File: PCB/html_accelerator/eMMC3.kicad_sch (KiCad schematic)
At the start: 16 parts, among them U2 AU6438BS, U5 EMMC_4G, U6 EMMC_4G, U7 EMMC_4G, Y1 12MHz

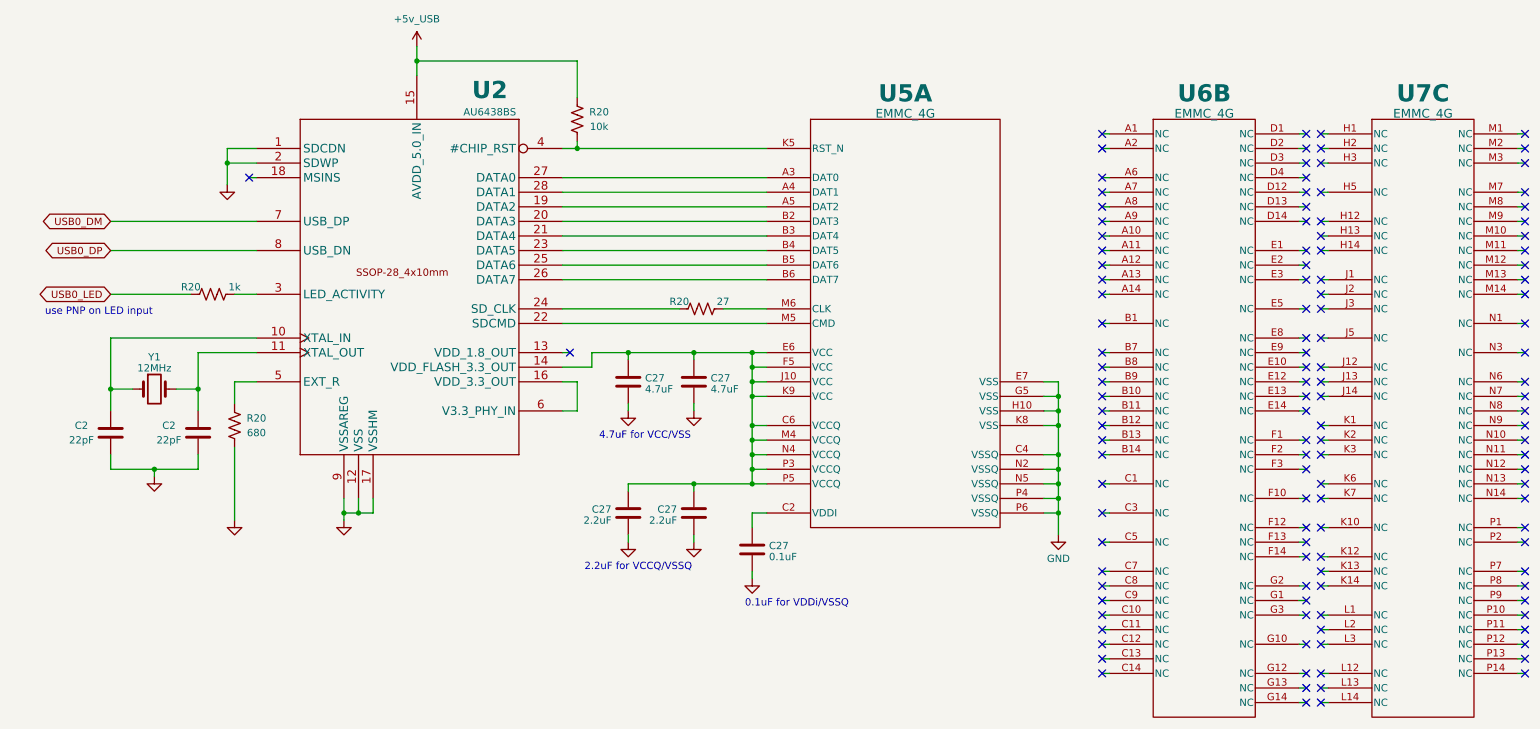
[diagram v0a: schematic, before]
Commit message: EMMC symbols and netlist
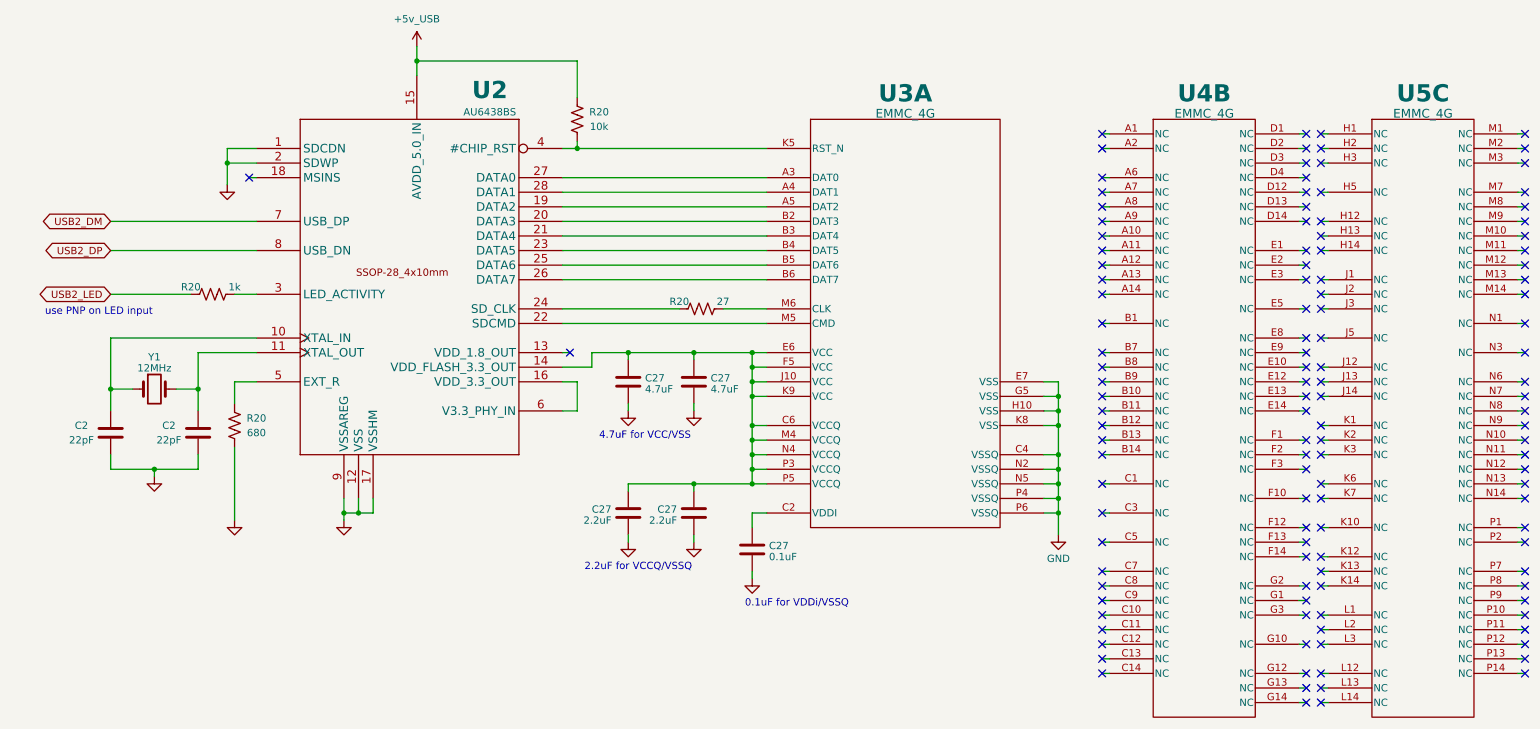
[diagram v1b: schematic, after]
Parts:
- removed C2 (x2): 22pF, symbol Device:C
- removed C27 (x2): 2.2uF, symbol Device:C
- removed C27 (x2): 4.7uF, symbol Device:C
- removed C27: 0.1uF, symbol Device:C
- removed R20: 10k, symbol Device:R_US
- removed R20: 680, symbol Device:R_US
- removed R20: 1k, symbol Device:R_US
- removed R20: 27, symbol Device:R_US
- removed U5, U6, U7: EMMC_4G, EMMC04G-M627-X03U_KNT, symbol html_accel_Symbols:EMMC_4G
- added C2 (x2): 22pF, symbol Device:C
- added C27 (x2): 2.2uF, symbol Device:C
- added C27: 0.1uF, symbol Device:C
- added C27 (x2): 4.7uF, symbol Device:C
- added R20: 680, symbol Device:R_US
- added R20: 1k, symbol Device:R_US
- added R20: 10k, symbol Device:R_US
- added R20: 27, symbol Device:R_US
- added U3, U4, U5: EMMC_4G, EMMC04G-M627-X03U_KNT, symbol html_accel_Symbols:EMMC_4G
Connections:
- net +3V3: now also R20.1
- net GND: now also C2.2, C2.2, C27.2, C27.2, C27.2, C27.2, C27.2, R20.2, U3.C4 (VSSQ), U3.E7 (VSS), U3.G5 (VSS), U3.H10 (VSS), U3.K8 (VSS), U3.N2 (VSSQ), U3.N5 (VSSQ), U3.P4 (VSSQ), U3.P6 (VSSQ)
- net at U2.4 (#CHIP_RST): now also R20.2, U3.K5 (RST_N)
- net at U2.27 (DATA0): now also U3.A3 (DAT0)
- net at U2.28 (DATA1): now also U3.A4 (DAT1)
- net at U2.19 (DATA2): now also U3.A5 (DAT2)
- net at U2.20 (DATA3): now also U3.B2 (DAT3)
- net at U2.21 (DATA4): now also U3.B3 (DAT4)
- net at U2.23 (DATA5): now also U3.B4 (DAT5)
- net at U2.25 (DATA6): now also U3.B5 (DAT6)
- net at U2.26 (DATA7): now also U3.B6 (DAT7)
- net at U2.14 (VDD_FLASH_3.3_OUT): now also C27.1, C27.1, C27.1, C27.1, U3.C6 (VCCQ), U3.E6 (VCC), U3.F5 (VCC), U3.J10 (VCC), U3.K9 (VCC), U3.M4 (VCCQ), U3.N4 (VCCQ), U3.P3 (VCCQ), U3.P5 (VCCQ)
- net at U2.22 (SDCMD): now also U3.M5 (CMD)
- net at U2.5 (EXT_R): now also R20.1
- net at U2.11 (XTAL_OUT), Y1.2: now also C2.1
- net at U2.10 (XTAL_IN), Y1.1: now also C2.1
- net at U2.3 (LED_ACTIVITY): now also R20.2
- net at U2.24 (SD_CLK): now also R20.1
- net USB0_DM renamed USB2_DM
- net USB0_DP renamed USB2_DP
- new net: C27.1, U3.C2 (VDDI)
- new net: R20.2, U3.M6 (CLK)
- new net USB2_LED: R20.1

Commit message: 3d part models, PCB netlist imported
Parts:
- C2, C27: footprint (none) -> Capacitor_SMD:C_0805_2012Metric_Pad1.18x1.45mm_HandSolder
- R20: footprint (none) -> Resistor_SMD:R_0805_2012Metric_Pad1.20x1.40mm_HandSolder
- U3, U4, U5: footprint EMMC04G-M627-X03U_KNT -> html_accel_footprints:EMMC04G-M627-X03U_KNT
- Y1: footprint (none) -> Crystal:Crystal_SMD_HC49-SD
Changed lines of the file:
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@@
       (effects (font (size 1.524 1.524)))
     )
-    (property "Footprint" "EMMC04G-M627-X03U_KNT" (at 231.14 48.26 0)
+    (property "Footprint" "html_accel_footprints:EMMC04G-M627-X03U_KNT" (at 231.14 48.26 0)
       (effects (font (size 1.27 1.27) italic) hide)
     )
@@
       (effects (font (size 1.27 1.27)))
     )
-    (property "Footprint" "" (at 48.5648 106.68 0)
+    (property "Footprint" "Capacitor_SMD:C_0805_2012Metric_Pad1.18x1.45mm_HandSolder" (at 48.5648 106.68 0)
       (effects (font (size 1.27 1.27)) hide)
     )
@@
       (effects (font (size 1.27 1.27)))
     )
-    (property "Footprint" "" (at 56.896 101.854 90)
+    (property "Footprint" "Resistor_SMD:R_0805_2012Metric_Pad1.20x1.40mm_HandSolder" (at 56.896 101.854 90)
       (effects (font (size 1.27 1.27)) hide)
     )
@@
       (effects (font (size 1.27 1.27)) (justify left))
     )
-    (property "Footprint" "" (at 134.9248 120.65 0)
+    (property "Footprint" "Capacitor_SMD:C_0805_2012Metric_Pad1.18x1.45mm_HandSolder" (at 134.9248 120.65 0)
       (effects (font (size 1.27 1.27)) hide)
     )
@@
       (effects (font (size 1.27 1.27)))
     )
-    (property "Footprint" "" (at 52.324 77.724 90)
+    (property "Footprint" "Resistor_SMD:R_0805_2012Metric_Pad1.20x1.40mm_HandSolder" (at 52.324 77.724 90)
       (effects (font (size 1.27 1.27)) hide)
     )
@@
       (effects (font (size 1.27 1.27)) (justify left))
     )
-    (property "Footprint" "" (at 147.0152 127 0)
+    (property "Footprint" "Capacitor_SMD:C_0805_2012Metric_Pad1.18x1.45mm_HandSolder" (at 147.0152 127 0)
       (effects (font (size 1.27 1.27)) hide)
     )
@@
       (effects (font (size 1.524 1.524)))
     )
-    (property "Footprint" "EMMC04G-M627-X03U_KNT" (at 171.45 48.26 0)
+    (property "Footprint" "html_accel_footprints:EMMC04G-M627-X03U_KNT" (at 171.45 48.26 0)
       (effects (font (size 1.27 1.27) italic) hide)
     )
@@
       (effects (font (size 1.27 1.27)))
     )
-    (property "Footprint" "" (at 33.3248 106.68 0)
+    (property "Footprint" "Capacitor_SMD:C_0805_2012Metric_Pad1.18x1.45mm_HandSolder" (at 33.3248 106.68 0)
       (effects (font (size 1.27 1.27)) hide)
     )
@@
       (effects (font (size 1.524 1.524)))
     )
-    (property "Footprint" "EMMC04G-M627-X03U_KNT" (at 269.24 48.26 0)
+    (property "Footprint" "html_accel_footprints:EMMC04G-M627-X03U_KNT" (at 269.24 48.26 0)
       (effects (font (size 1.27 1.27) italic) hide)
     )
@@
       (effects (font (size 1.27 1.27)))
     )
-    (property "Footprint" "" (at 116.586 48.514 90)
+    (property "Footprint" "Resistor_SMD:R_0805_2012Metric_Pad1.20x1.40mm_HandSolder" (at 116.586 48.514 90)
       (effects (font (size 1.27 1.27)) hide)
     )
@@
       (effects (font (size 1.27 1.27)) (justify left))
     )
-    (property "Footprint" "" (at 123.4948 120.65 0)
+    (property "Footprint" "Capacitor_SMD:C_0805_2012Metric_Pad1.18x1.45mm_HandSolder" (at 123.4948 120.65 0)
       (effects (font (size 1.27 1.27)) hide)
     )
@@
       (effects (font (size 1.27 1.27)))
     )
-    (property "Footprint" "" (at 41.91 95.25 0)
-      (effects (font (size 1.27 1.27)) hide)
-    )
-    (property "Datasheet" "~" (at 41.91 95.25 0)
+    (property "Footprint" "Crystal:Crystal_SMD_HC49-SD" (at 41.91 95.25 0)
+      (effects (font (size 1.27 1.27)) hide)
+    )
+    (property "Datasheet" "12M20P2/49SMT" (at 41.91 95.25 0)
       (effects (font (size 1.27 1.27)) hide)
     )
@@
       (effects (font (size 1.27 1.27)) (justify left))
     )
-    (property "Footprint" "" (at 136.8552 97.79 0)
+    (property "Footprint" "Capacitor_SMD:C_0805_2012Metric_Pad1.18x1.45mm_HandSolder" (at 136.8552 97.79 0)
       (effects (font (size 1.27 1.27)) hide)
     )
@@
       (effects (font (size 1.27 1.27)))
     )
-    (property "Footprint" "" (at 137.414 80.264 90)
+    (property "Footprint" "Resistor_SMD:R_0805_2012Metric_Pad1.20x1.40mm_HandSolder" (at 137.414 80.264 90)
       (effects (font (size 1.27 1.27)) hide)
     )
@@
       (effects (font (size 1.27 1.27)) (justify left))
     )
-    (property "Footprint" "" (at 125.4252 97.79 0)
-      (effects (font (size 1.27 1.27)) hide)
-    )
+    (property "Footprint" "Capacitor_SMD:C_0805_2012Metric_Pad1.18x1.45mm_HandSolder" (at 125.4252 97.79 0)
+      (effects (font (size 1.27 1.27)) hide)
+    )

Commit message: placement updates
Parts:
- Y1: footprint Crystal:Crystal_SMD_HC49-SD -> Crystal:Crystal_SMD_3225-4Pin_3.2x2.5mm
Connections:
- net +3V3 renamed +5V
- no-connect marks 125 -> 2

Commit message: layout and 3d updates
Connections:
- net DATA_2: now reaches U2.19 (DATA2), U3.A5 (DAT2)
- net DATA_3: now reaches U2.20 (DATA3), U3.B2 (DAT3)
- net DATA_4: now reaches U2.21 (DATA4), U3.B3 (DAT4)
- net DATA_5: now reaches U2.23 (DATA5), U3.B4 (DAT5)
- net DATA_6: now reaches U2.25 (DATA6), U3.B5 (DAT6)
- net DATA_7: now reaches U2.26 (DATA7), U3.B6 (DAT7)
- net DATA_0: now reaches U2.27 (DATA0), U3.A3 (DAT0)
- net DATA_1: now reaches U2.28 (DATA1), U3.A4 (DAT1)
- net USB2_DM renamed 90_USB2_D_P
- net USB2_DP renamed 90_USB2_D_N
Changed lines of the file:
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@@
+    (effects (font (size 1.27 1.27)) (justify left bottom))
+  )
+  (label "DATA_0" (at 115.57 58.42 0) (fields_autoplaced)
+    (effects (font (size 1.27 1.27)) (justify left bottom))
+  )
+  (label "DATA_1" (at 115.57 60.96 0) (fields_autoplaced)
+    (effects (font (size 1.27 1.27)) (justify left bottom))
+  )
+  (label "DATA_2" (at 115.57 63.5 0) (fields_autoplaced)
+    (effects (font (size 1.27 1.27)) (justify left bottom))
+  )
+  (label "DATA_4" (at 115.57 68.58 0) (fields_autoplaced)
+    (effects (font (size 1.27 1.27)) (justify left bottom))
+  )
+  (label "DATA_7" (at 115.57 76.2 0) (fields_autoplaced)
+    (effects (font (size 1.27 1.27)) (justify left bottom))
+  )
+  (label "DATA_5" (at 115.57 71.12 0) (fields_autoplaced)
+    (effects (font (size 1.27 1.27)) (justify left bottom))
+  )
+  (label "DATA_6" (at 115.57 73.66 0) (fields_autoplaced)
+    (effects (font (size 1.27 1.27)) (justify left bottom))
+  )
+  (label "DATA_3" (at 115.57 66.04 0) (fields_autoplaced)
     (effects (font (size 1.27 1.27)) (justify left bottom))
   )
@@
     )
   )
-  (global_label "USB2_DM" (shape bidirectional) (at 34.29 66.04 180) (fields_autoplaced)
+  (global_label "90_USB2_D_P" (shape bidirectional) (at 34.29 66.04 180) (fields_autoplaced)
     (effects (font (size 1.27 1.27)) (justify right))
-    (property "Intersheetrefs" "${INTERSHEET_REFS}" (at 21.5644 66.04 0)
+    (property "Intersheetrefs" "${INTERSHEET_REFS}" (at 17.3916 66.04 0)
       (effects (font (size 1.27 1.27)) (justify right))
     )
   )
-  (global_label "USB2_DP" (shape bidirectional) (at 34.29 71.12 180) (fields_autoplaced)
+  (global_label "90_USB2_D_N" (shape bidirectional) (at 34.29 71.12 180) (fields_autoplaced)
     (effects (font (size 1.27 1.27)) (justify right))
-    (property "Intersheetrefs" "${INTERSHEET_REFS}" (at 21.7458 71.12 0)
+    (property "Intersheetrefs" "${INTERSHEET_REFS}" (at 17.3311 71.12 0)
       (effects (font (size 1.27 1.27)) (justify right))
     )

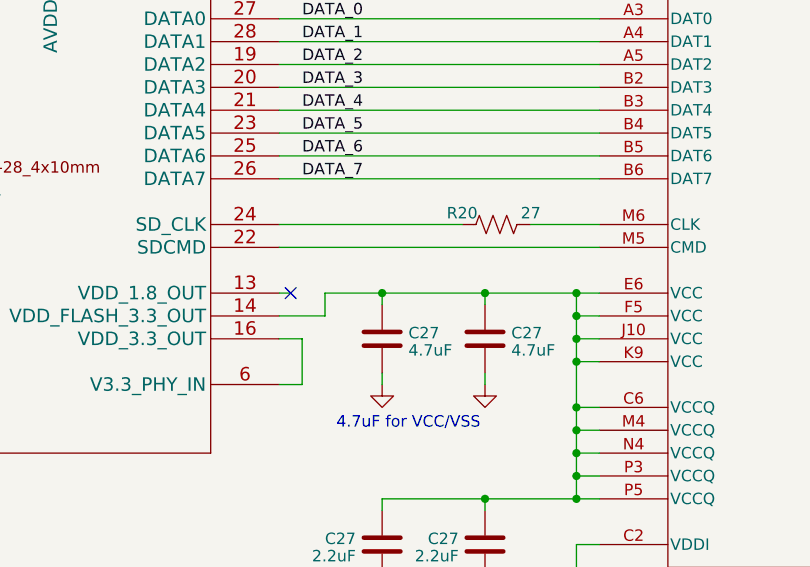
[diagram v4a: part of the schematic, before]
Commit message: impedance controlled nets
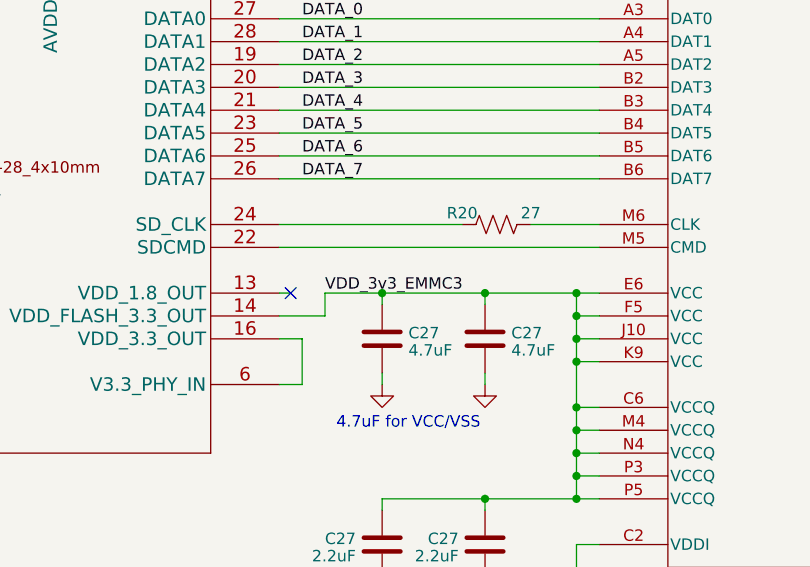
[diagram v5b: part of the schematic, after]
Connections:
- net VDD_3v3_EMMC3: now reaches C27.1, C27.1, C27.1, C27.1, U2.14 (VDD_FLASH_3.3_OUT), U3.C6 (VCCQ), U3.E6 (VCC), U3.F5 (VCC), U3.J10 (VCC), U3.K9 (VCC), U3.M4 (VCCQ), U3.N4 (VCCQ), U3.P3 (VCCQ), U3.P5 (VCCQ)
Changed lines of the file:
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@@
+    (effects (font (size 1.27 1.27)) (justify left bottom))
+  )
+  (label "VDD_3v3_EMMC3" (at 118.11 88.9 0) (fields_autoplaced)
     (effects (font (size 1.27 1.27)) (justify left bottom))
   )

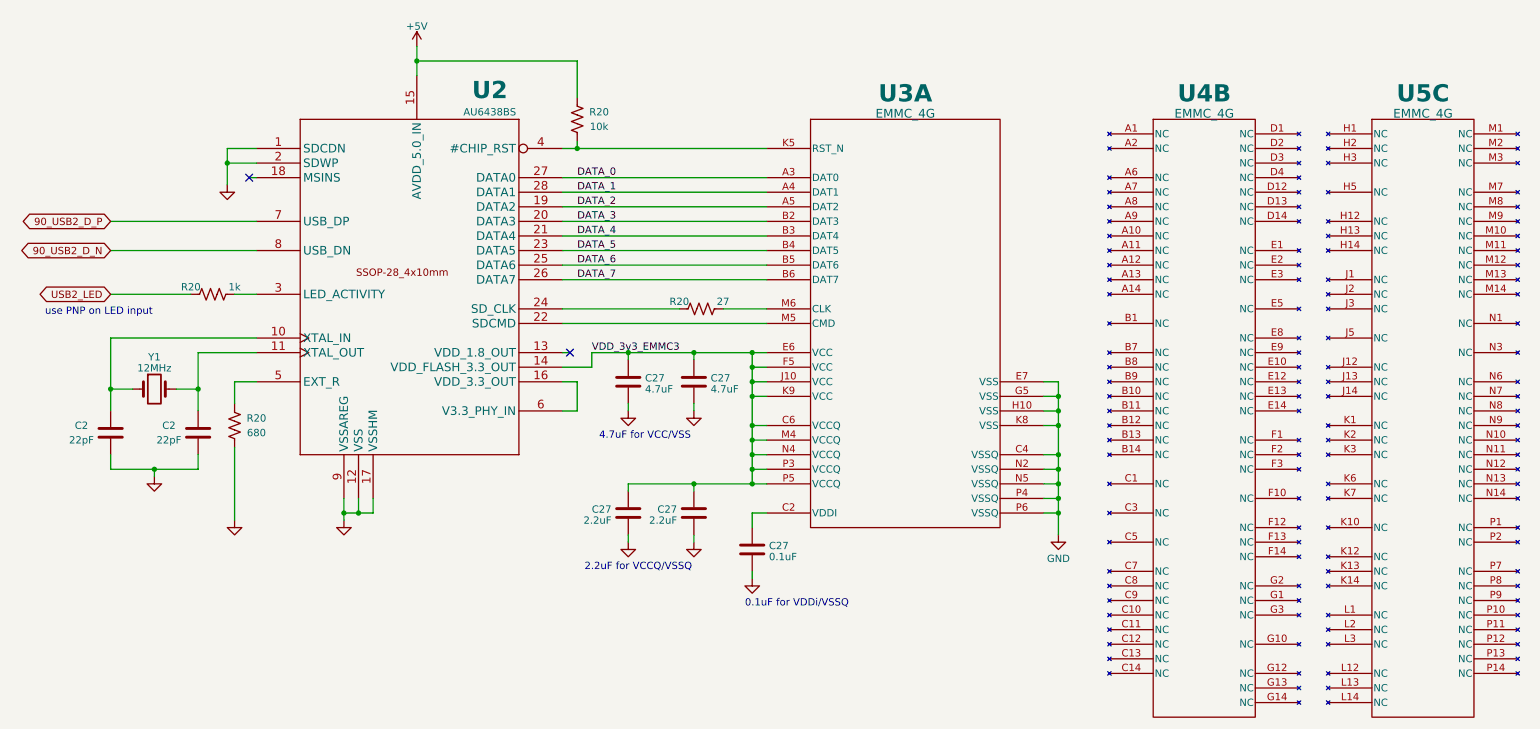
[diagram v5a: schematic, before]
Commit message: constraints for impedance control
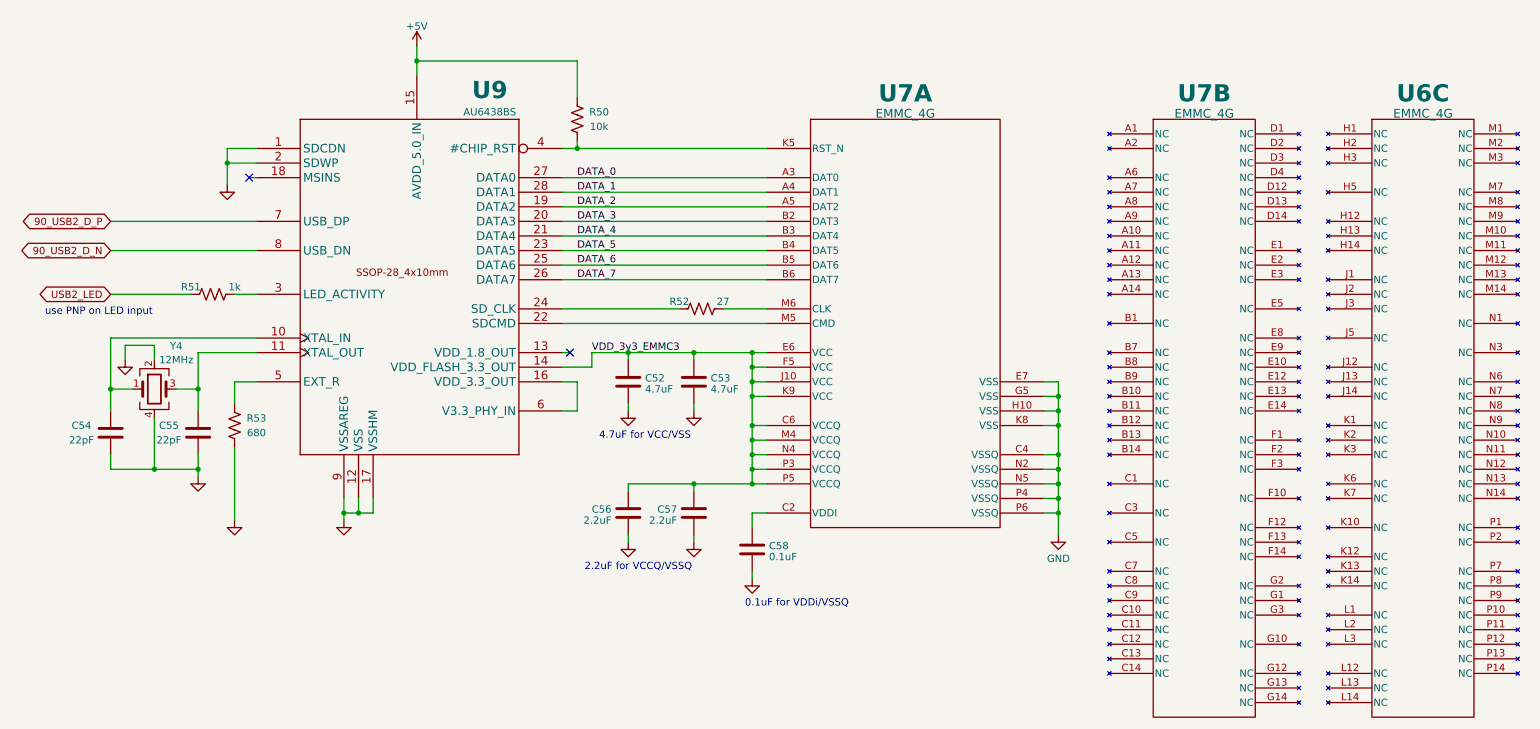
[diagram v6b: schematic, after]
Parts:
- removed Y1: 12MHz, Crystal:Crystal_SMD_3225-4Pin_3.2x2.5mm, symbol Device:Crystal
- added Y4: 12MHz, Crystal:Crystal_SMD_3225-4Pin_3.2x2.5mm, symbol Device:Crystal_GND24
- renumbered C27 to C52, C27 to C53, C2 to C54, C2 to C55, C27 to C56, C27 to C57, C27 to C58, R20 to R50, R20 to R51, R20 to R52, R20 to R53, U5 to U6, U4 to U7, U3 to U7, U2 to U9
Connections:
- net GND: now also Y4.2, Y4.4
- net at C54.1, U9.10 (XTAL_IN): now also Y4.1
- net at C55.1, U9.11 (XTAL_OUT): now also Y4.3
